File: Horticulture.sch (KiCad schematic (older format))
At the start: 59 parts, among them J2 Conn_02x05_Odd_Even, J3 Conn_01x04_Male, J4 Conn_01x04_Male, SW1 SW-I2C, SW2 Rotary_Encoder_Switch, U1 TLE4309, U2 TLE4309, U3 TLE4309, U4 TLE4309, U6 STM32F030F4Px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

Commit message: Added debounceresistors to Encoder
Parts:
- added R? (x6): 10K2, symbol Device:R_Small
- VR1: symbol Regulator_Switching:TPS560430X3FDBV -> Horticulture-rescue:TPS560430X3FDBV-Regulator_Switching
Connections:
- net +3.3V: now also R?.2, R?.2, R?.2
- net Enc-A: now also R?.2; no longer C3.1, SW2.A
- net Enc-B: now also R?.2; no longer C4.2, SW2.B
- net Enc-bt1: now also R?.1; no longer C5.1, SW2.S1
- new net: C3.1, R?.1, R?.1, SW2.A
- new net: C4.2, R?.1, R?.1, SW2.B
- new net: C5.1, R?.1, R?.2, SW2.S1
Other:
- moved on the sheet: C3, C4
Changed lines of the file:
@@
 L Device:C_Small C4
 U 1 1 5F1C0369
-P 10250 6600
-F 0 "C4" H 10342 6646 50  0000 L CNN
-F 1 "100nF" H 10342 6555 50  0000 L CNN
-F 2 "Capacitor_SMD:C_0603_1608Metric" H 10250 6600 50  0001 C CNN
-F 3 "~" H 10250 6600 50  0001 C CNN
-	1    10250 6600
+P 10600 6600
+F 0 "C4" H 10692 6646 50  0000 L CNN
+F 1 "100nF" H 10692 6555 50  0000 L CNN
+F 2 "Capacitor_SMD:C_0603_1608Metric" H 10600 6600 50  0001 C CNN
+F 3 "~" H 10600 6600 50  0001 C CNN
+	1    10600 6600
 	1    0    0    -1
 $EndComp
@@
 L Device:C_Small C3
 U 1 1 5F1C0EDC
-P 10250 6400
-F 0 "C3" H 10342 6446 50  0000 L CNN
-F 1 "100nF" H 10342 6355 50  0000 L CNN
-F 2 "Capacitor_SMD:C_0603_1608Metric" H 10250 6400 50  0001 C CNN
-F 3 "~" H 10250 6400 50  0001 C CNN
-	1    10250 6400
-	1    0    0    -1
-$EndComp
-Wire Wire Line
-	10250 6500 10700 6500
-Connection ~ 10250 6500
-Wire Wire Line
-	10250 6300 10700 6300
+P 10600 6400
+F 0 "C3" H 10692 6446 50  0000 L CNN
+F 1 "100nF" H 10692 6355 50  0000 L CNN
+F 2 "Capacitor_SMD:C_0603_1608Metric" H 10600 6400 50  0001 C CNN
+F 3 "~" H 10600 6400 50  0001 C CNN
+	1    10600 6400
+	1    0    0    -1
+$EndComp
 Wire Wire Line
 	10700 6300 10700 6400
 Wire Wire Line
 	10700 6600 10700 6700
-Wire Wire Line
-	10700 6700 10250 6700
 $Comp
 L Device:C_Small C5
@@
 Text GLabel 10250 6300 0    50   Input ~ 0
 Enc-A
-Wire Wire Line
-	11350 6400 11550 6400
 Connection ~ 11350 6400
-Wire Wire Line
-	10050 6500 10250 6500
 Text GLabel 8650 7150 2    50   Input ~ 0
 Enc-A
@@
 $EndComp
 $Comp
-L Regulator_Switching:TPS560430X3FDBV VR1
+L Horticulture-rescue:TPS560430X3FDBV-Regulator_Switching VR1
 U 1 1 5F7BCC88
 P 4300 7500
@@
 	0    1    1    0
 $EndComp
+$Comp
+L Device:R_Small R?
+U 1 1 5FBECB79
+P 10450 6300
+F 0 "R?" V 10254 6300 50  0000 C CNN
+F 1 "10K2" V 10345 6300 50  0000 C CNN
+F 2 "" H 10450 6300 50  0001 C CNN
+F 3 "~" H 10450 6300 50  0001 C CNN
+	1    10450 6300
+	0    1    1    0
+$EndComp
+$Comp
+L Device:R_Small R?
+U 1 1 5FBF75E8
+P 10450 6700
+F 0 "R?" V 10254 6700 50  0000 C CNN
+F 1 "10K2" V 10345 6700 50  0000 C CNN
+F 2 "" H 10450 6700 50  0001 C CNN
+F 3 "~" H 10450 6700 50  0001 C CNN
+	1    10450 6700
+	0    1    1    0
+$EndComp
+Wire Wire Line
+	10550 6700 10600 6700
+Wire Wire Line
+	10700 6300 10600 6300
+Wire Wire Line
+	10350 6300 10250 6300
+Wire Wire Line
+	10250 6700 10350 6700
+Connection ~ 10600 6300
+Wire Wire Line
+	10600 6300 10550 6300
+Connection ~ 10600 6500
+Wire Wire Line
+	10600 6500 10700 6500
+Connection ~ 10600 6700
+Wire Wire Line
+	10600 6700 10650 6700
+Wire Wire Line
+	10050 6500 10600 6500
+Text GLabel 11000 6000 1    50   Input ~ 0
++3.3V
+$Comp
+L Device:R_Small R?
+U 1 1 5FC256FB
+P 11350 6200
+F 0 "R?" H 11291 6154 50  0000 R CNN
+F 1 "10K2" H 11291 6245 50  0000 R CNN
+F 2 "" H 11350 6200 50  0001 C CNN
+F 3 "~" H 11350 6200 50  0001 C CNN
+	1    11350 6200
+	-1   0    0    1
+$EndComp
+$Comp
+L Device:R_Small R?
+U 1 1 5FC2721C
+P 10550 6050
+F 0 "R?" H 10491 6004 50  0000 R CNN
+F 1 "10K2" H 10491 6095 50  0000 R CNN
+F 2 "" H 10550 6050 50  0001 C CNN
+F 3 "~" H 10550 6050 50  0001 C CNN
+	1    10550 6050
+	-1   0    0    1
+$EndComp
+$Comp
+L Device:R_Small R?
+U 1 1 5FC27E8A
+P 10650 6050
+F 0 "R?" H 10591 6004 50  0000 R CNN
+F 1 "10K2" H 10591 6095 50  0000 R CNN
+F 2 "" H 10650 6050 50  0001 C CNN
+F 3 "~" H 10650 6050 50  0001 C CNN
+	1    10650 6050
+	-1   0    0    1
+$EndComp
+Wire Wire Line
+	10650 5950 10850 5950
+Wire Wire Line
+	10850 5950 10850 6000
+Wire Wire Line
+	11350 6000 11350 6100
+Wire Wire Line
+	10850 6000 11350 6000
+Wire Wire Line
+	11350 6300 11350 6400
+Wire Wire Line
+	10650 5950 10550 5950
+Connection ~ 10650 5950
+Wire Wire Line
+	10550 6150 10550 6300
+Connection ~ 10550 6300
+Wire Wire Line
+	10650 6150 10650 6700
+Connection ~ 10650 6700
+Wire Wire Line
+	10650 6700 10700 6700
+$Comp
+L Device:R_Small R?
+U 1 1 5FC4F638
+P 11450 6400
+F 0 "R?" V 11254 6400 50  0000 C CNN
+F 1 "10K2" V 11345 6400 50  0000 C CNN
+F 2 "" H 11450 6400 50  0001 C CNN
+F 3 "~" H 11450 6400 50  0001 C CNN
+	1    11450 6400
+	0    1    1    0
+$EndComp

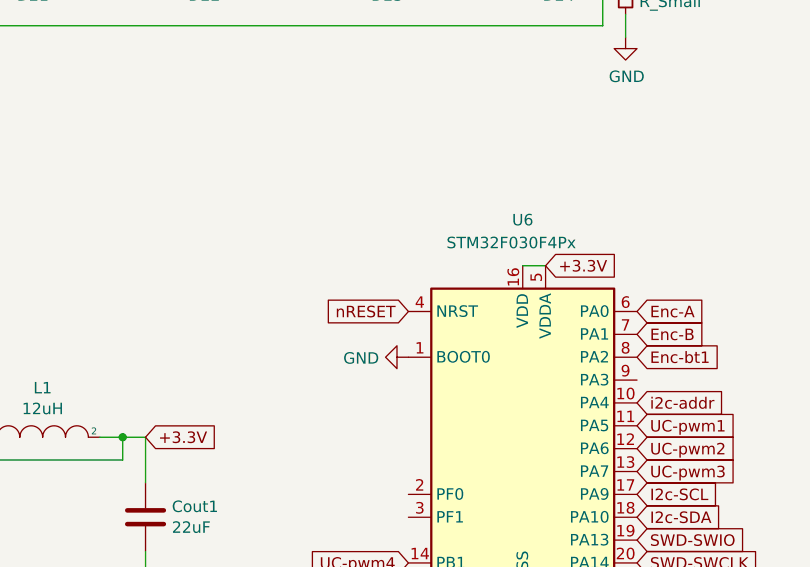
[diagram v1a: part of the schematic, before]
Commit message: Pullup to nRESET
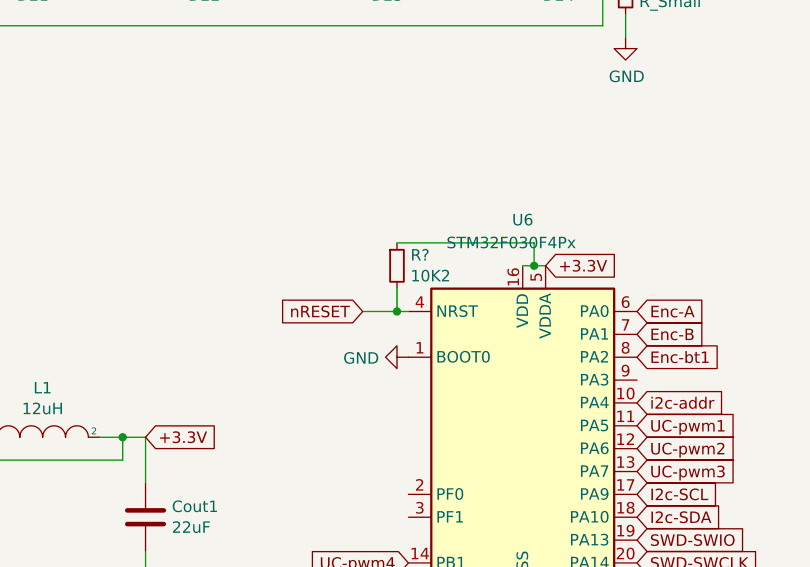
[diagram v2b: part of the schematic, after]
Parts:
- added R?: 10K2, symbol Device:R_Small
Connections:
- net +3.3V: now also R?.1
- net nRESET: now also R?.2
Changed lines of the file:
@@
 	12750 8000 12950 8000
 Connection ~ 12950 8000
-Text GLabel 7650 7150 0    50   Input ~ 0
+Text GLabel 7450 7150 0    50   Input ~ 0
 nRESET
 Text GLabel 8650 8250 2    50   Input ~ 0
@@
 $EndComp
 Wire Wire Line
-	8250 6950 8150 6950
+	8250 6950 8200 6950
 $Comp
 L MCU_ST_STM32F0:STM32F030F4Px U6
@@
 	0    1    1    0
 $EndComp
+$Comp
+L Device:R_Small R?
+U 1 1 5FC6BC68
+P 7600 6950
+F 0 "R?" H 7659 6996 50  0000 L CNN
+F 1 "10K2" H 7659 6905 50  0000 L CNN
+F 2 "" H 7600 6950 50  0001 C CNN
+F 3 "~" H 7600 6950 50  0001 C CNN
+	1    7600 6950
+	1    0    0    -1
+$EndComp
+Wire Wire Line
+	7450 7150 7600 7150
+Wire Wire Line
+	7600 7050 7600 7150
+Connection ~ 7600 7150
+Wire Wire Line
+	7600 7150 7650 7150
+Wire Wire Line
+	7600 6850 8200 6850
+Wire Wire Line
+	8200 6850 8200 6950
+Connection ~ 8200 6950
+Wire Wire Line
+	8200 6950 8150 6950
 $EndSCHEMATC

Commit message: Added footprint to new resistors
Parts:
- R10, R7, R8, R9: footprint Resistor_SMD:R_0805_2012Metric_Pad1.15x1.40mm_HandSolder -> Resistor_SMD:R_0603_1608Metric
- R11, R12, R13, R14, R15, R16, R17: renamed from R?; footprint (none) -> Resistor_SMD:R_0603_1608Metric
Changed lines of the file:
@@
 F 0 "R10" H 2370 5996 50  0000 L CNN
 F 1 "10k" H 2370 5905 50  0000 L CNN
-F 2 "Resistor_SMD:R_0805_2012Metric_Pad1.15x1.40mm_HandSolder" V 2230 5950 50  0001 C CNN
+F 2 "Resistor_SMD:R_0603_1608Metric" V 2230 5950 50  0001 C CNN
 F 3 "~" H 2300 5950 50  0001 C CNN
 	1    2300 5950
@@
 F 0 "R9" H 2370 4496 50  0000 L CNN
 F 1 "10k" H 2370 4405 50  0000 L CNN
-F 2 "Resistor_SMD:R_0805_2012Metric_Pad1.15x1.40mm_HandSolder" V 2230 4450 50  0001 C CNN
+F 2 "Resistor_SMD:R_0603_1608Metric" V 2230 4450 50  0001 C CNN
 F 3 "~" H 2300 4450 50  0001 C CNN
 	1    2300 4450
@@
 F 0 "R8" H 2370 3096 50  0000 L CNN
 F 1 "10k" H 2370 3005 50  0000 L CNN
-F 2 "Resistor_SMD:R_0805_2012Metric_Pad1.15x1.40mm_HandSolder" V 2230 3050 50  0001 C CNN
+F 2 "Resistor_SMD:R_0603_1608Metric" V 2230 3050 50  0001 C CNN
 F 3 "~" H 2300 3050 50  0001 C CNN
 	1    2300 3050
@@
 F 0 "R7" H 2370 1796 50  0000 L CNN
 F 1 "10k" H 2370 1705 50  0000 L CNN
-F 2 "Resistor_SMD:R_0805_2012Metric_Pad1.15x1.40mm_HandSolder" V 2230 1750 50  0001 C CNN
+F 2 "Resistor_SMD:R_0603_1608Metric" V 2230 1750 50  0001 C CNN
 F 3 "~" H 2300 1750 50  0001 C CNN
 	1    2300 1750
@@
 $EndComp
 $Comp
-L Device:R_Small R?
+L Device:R_Small R12
 U 1 1 5FBECB79
 P 10450 6300
-F 0 "R?" V 10254 6300 50  0000 C CNN
+F 0 "R12" V 10254 6300 50  0000 C CNN
 F 1 "10K2" V 10345 6300 50  0000 C CNN
-F 2 "" H 10450 6300 50  0001 C CNN
+F 2 "Resistor_SMD:R_0603_1608Metric" H 10450 6300 50  0001 C CNN
 F 3 "~" H 10450 6300 50  0001 C CNN
 	1    10450 6300
@@
 $EndComp
 $Comp
-L Device:R_Small R?
+L Device:R_Small R13
 U 1 1 5FBF75E8
 P 10450 6700
-F 0 "R?" V 10254 6700 50  0000 C CNN
+F 0 "R13" V 10254 6700 50  0000 C CNN
 F 1 "10K2" V 10345 6700 50  0000 C CNN
-F 2 "" H 10450 6700 50  0001 C CNN
+F 2 "Resistor_SMD:R_0603_1608Metric" H 10450 6700 50  0001 C CNN
 F 3 "~" H 10450 6700 50  0001 C CNN
 	1    10450 6700
@@
 +3.3V
 $Comp
-L Device:R_Small R?
+L Device:R_Small R16
 U 1 1 5FC256FB
 P 11350 6200
-F 0 "R?" H 11291 6154 50  0000 R CNN
+F 0 "R16" H 11291 6154 50  0000 R CNN
 F 1 "10K2" H 11291 6245 50  0000 R CNN
-F 2 "" H 11350 6200 50  0001 C CNN
+F 2 "Resistor_SMD:R_0603_1608Metric" H 11350 6200 50  0001 C CNN
 F 3 "~" H 11350 6200 50  0001 C CNN
 	1    11350 6200
@@
 $EndComp
 $Comp
-L Device:R_Small R?
+L Device:R_Small R14
 U 1 1 5FC2721C
 P 10550 6050
-F 0 "R?" H 10491 6004 50  0000 R CNN
+F 0 "R14" H 10491 6004 50  0000 R CNN
 F 1 "10K2" H 10491 6095 50  0000 R CNN
-F 2 "" H 10550 6050 50  0001 C CNN
+F 2 "Resistor_SMD:R_0603_1608Metric" H 10550 6050 50  0001 C CNN
 F 3 "~" H 10550 6050 50  0001 C CNN
 	1    10550 6050
@@
 $EndComp
 $Comp
-L Device:R_Small R?
+L Device:R_Small R15
 U 1 1 5FC27E8A
 P 10650 6050
-F 0 "R?" H 10591 6004 50  0000 R CNN
+F 0 "R15" H 10591 6004 50  0000 R CNN
 F 1 "10K2" H 10591 6095 50  0000 R CNN
-F 2 "" H 10650 6050 50  0001 C CNN
+F 2 "Resistor_SMD:R_0603_1608Metric" H 10650 6050 50  0001 C CNN
 F 3 "~" H 10650 6050 50  0001 C CNN
 	1    10650 6050
@@
 	10650 6700 10700 6700
 $Comp
-L Device:R_Small R?
+L Device:R_Small R17
 U 1 1 5FC4F638
 P 11450 6400
-F 0 "R?" V 11254 6400 50  0000 C CNN
+F 0 "R17" V 11254 6400 50  0000 C CNN
 F 1 "10K2" V 11345 6400 50  0000 C CNN
-F 2 "" H 11450 6400 50  0001 C CNN
+F 2 "Resistor_SMD:R_0603_1608Metric" H 11450 6400 50  0001 C CNN
 F 3 "~" H 11450 6400 50  0001 C CNN
 	1    11450 6400
@@
 $EndComp
 $Comp
-L Device:R_Small R?
+L Device:R_Small R11
 U 1 1 5FC6BC68
 P 7600 6950
-F 0 "R?" H 7659 6996 50  0000 L CNN
+F 0 "R11" H 7659 6996 50  0000 L CNN
 F 1 "10K2" H 7659 6905 50  0000 L CNN
-F 2 "" H 7600 6950 50  0001 C CNN
+F 2 "Resistor_SMD:R_0603_1608Metric" H 7600 6950 50  0001 C CNN
 F 3 "~" H 7600 6950 50  0001 C CNN
 	1    7600 6950

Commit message: Added footprint to new resistors
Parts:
- R10, R11, R12, R13, R14, R15, R16, R17, R7, R8, R9: footprint Resistor_SMD:R_0603_1608Metric -> Resistor_SMD:R_0402_1005Metric
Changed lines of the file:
@@
 F 0 "R10" H 2370 5996 50  0000 L CNN
 F 1 "10k" H 2370 5905 50  0000 L CNN
-F 2 "Resistor_SMD:R_0603_1608Metric" V 2230 5950 50  0001 C CNN
+F 2 "Resistor_SMD:R_0402_1005Metric" V 2230 5950 50  0001 C CNN
 F 3 "~" H 2300 5950 50  0001 C CNN
 	1    2300 5950
@@
 F 0 "R9" H 2370 4496 50  0000 L CNN
 F 1 "10k" H 2370 4405 50  0000 L CNN
-F 2 "Resistor_SMD:R_0603_1608Metric" V 2230 4450 50  0001 C CNN
+F 2 "Resistor_SMD:R_0402_1005Metric" V 2230 4450 50  0001 C CNN
 F 3 "~" H 2300 4450 50  0001 C CNN
 	1    2300 4450
@@
 F 0 "R8" H 2370 3096 50  0000 L CNN
 F 1 "10k" H 2370 3005 50  0000 L CNN
-F 2 "Resistor_SMD:R_0603_1608Metric" V 2230 3050 50  0001 C CNN
+F 2 "Resistor_SMD:R_0402_1005Metric" V 2230 3050 50  0001 C CNN
 F 3 "~" H 2300 3050 50  0001 C CNN
 	1    2300 3050
@@
 F 0 "R7" H 2370 1796 50  0000 L CNN
 F 1 "10k" H 2370 1705 50  0000 L CNN
-F 2 "Resistor_SMD:R_0603_1608Metric" V 2230 1750 50  0001 C CNN
+F 2 "Resistor_SMD:R_0402_1005Metric" V 2230 1750 50  0001 C CNN
 F 3 "~" H 2300 1750 50  0001 C CNN
 	1    2300 1750
@@
 F 0 "R12" V 10254 6300 50  0000 C CNN
 F 1 "10K2" V 10345 6300 50  0000 C CNN
-F 2 "Resistor_SMD:R_0603_1608Metric" H 10450 6300 50  0001 C CNN
+F 2 "Resistor_SMD:R_0402_1005Metric" H 10450 6300 50  0001 C CNN
 F 3 "~" H 10450 6300 50  0001 C CNN
 	1    10450 6300
@@
 F 0 "R13" V 10254 6700 50  0000 C CNN
 F 1 "10K2" V 10345 6700 50  0000 C CNN
-F 2 "Resistor_SMD:R_0603_1608Metric" H 10450 6700 50  0001 C CNN
+F 2 "Resistor_SMD:R_0402_1005Metric" H 10450 6700 50  0001 C CNN
 F 3 "~" H 10450 6700 50  0001 C CNN
 	1    10450 6700
@@
 F 0 "R16" H 11291 6154 50  0000 R CNN
 F 1 "10K2" H 11291 6245 50  0000 R CNN
-F 2 "Resistor_SMD:R_0603_1608Metric" H 11350 6200 50  0001 C CNN
+F 2 "Resistor_SMD:R_0402_1005Metric" H 11350 6200 50  0001 C CNN
 F 3 "~" H 11350 6200 50  0001 C CNN
 	1    11350 6200
@@
 F 0 "R14" H 10491 6004 50  0000 R CNN
 F 1 "10K2" H 10491 6095 50  0000 R CNN
-F 2 "Resistor_SMD:R_0603_1608Metric" H 10550 6050 50  0001 C CNN
+F 2 "Resistor_SMD:R_0402_1005Metric" H 10550 6050 50  0001 C CNN
 F 3 "~" H 10550 6050 50  0001 C CNN
 	1    10550 6050
@@
 F 0 "R15" H 10591 6004 50  0000 R CNN
 F 1 "10K2" H 10591 6095 50  0000 R CNN
-F 2 "Resistor_SMD:R_0603_1608Metric" H 10650 6050 50  0001 C CNN
+F 2 "Resistor_SMD:R_0402_1005Metric" H 10650 6050 50  0001 C CNN
 F 3 "~" H 10650 6050 50  0001 C CNN
 	1    10650 6050
@@
 F 0 "R17" V 11254 6400 50  0000 C CNN
 F 1 "10K2" V 11345 6400 50  0000 C CNN
-F 2 "Resistor_SMD:R_0603_1608Metric" H 11450 6400 50  0001 C CNN
+F 2 "Resistor_SMD:R_0402_1005Metric" H 11450 6400 50  0001 C CNN
 F 3 "~" H 11450 6400 50  0001 C CNN
 	1    11450 6400
@@
 F 0 "R11" H 7659 6996 50  0000 L CNN
 F 1 "10K2" H 7659 6905 50  0000 L CNN
-F 2 "Resistor_SMD:R_0603_1608Metric" H 7600 6950 50  0001 C CNN
+F 2 "Resistor_SMD:R_0402_1005Metric" H 7600 6950 50  0001 C CNN
 F 3 "~" H 7600 6950 50  0001 C CNN
 	1    7600 6950

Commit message: 3.2.1- RC2. Fixes #4
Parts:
- added J1: Conn_01x04_Male, Connector_Molex:Molex_PicoBlade_53398-0471_1x04-1MP_P1.25mm_Vertical, symbol Connector:Conn_01x04_Male
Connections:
- net +3.3V: now also J1.4 (Pin_4)
- net GND: now also J1.1 (Pin_1)
- net I2c-SCL: now also J1.2 (Pin_2)
- net I2c-SDA: now also J1.3 (Pin_3)
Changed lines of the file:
@@
 Wire Wire Line
 	8200 6950 8150 6950
+Text GLabel 13650 5300 0    50   Input ~ 0
++3.3V
+$Comp
+L power:GND #PWR0126
+U 1 1 5FCD9F7E
+P 13650 5600
+F 0 "#PWR0126" H 13650 5350 50  0001 C CNN
+F 1 "GND" V 13655 5472 50  0000 R CNN
+F 2 "" H 13650 5600 50  0001 C CNN
+F 3 "" H 13650 5600 50  0001 C CNN
+	1    13650 5600
+	0    1    1    0
+$EndComp
+Text GLabel 13650 5500 0    50   Input ~ 0
+I2c-SCL
+Text GLabel 13650 5400 0    50   Input ~ 0
+I2c-SDA
+$Comp
+L Connector:Conn_01x04_Male J1
+U 1 1 5FCECF34
+P 13850 5500
+F 0 "J1" H 13822 5382 50  0000 R CNN
+F 1 "Conn_01x04_Male" H 13822 5473 50  0000 R CNN
+F 2 "Connector_Molex:Molex_PicoBlade_53398-0471_1x04-1MP_P1.25mm_Vertical" H 13850 5500 50  0001 C CNN
+F 3 "~" H 13850 5500 50  0001 C CNN
+	1    13850 5500
+	-1   0    0    1
+$EndComp
 $EndSCHEMATC
